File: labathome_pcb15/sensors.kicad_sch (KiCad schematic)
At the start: 23 parts, among them J12 TCS34725, J16 BMEx80, J19 BH1750, J20 CCS811, J21 QWIIC, J23 VL53L5x, J4 SCD4x, U12 AHT20, U14 BMP280, U19 DS18B20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

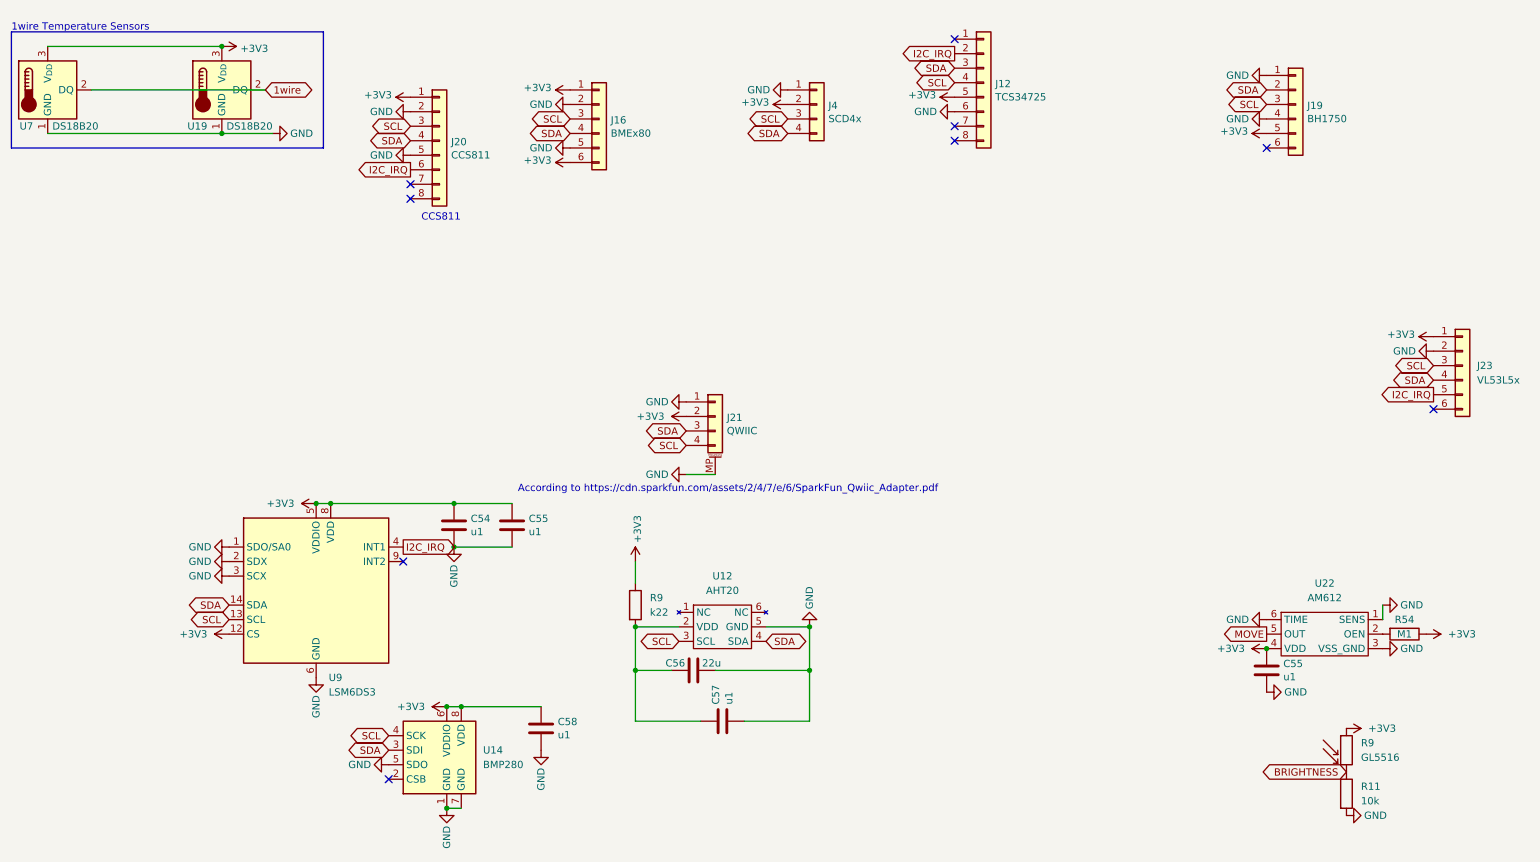
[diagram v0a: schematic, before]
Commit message: Updates in PCB, arduino test firmware
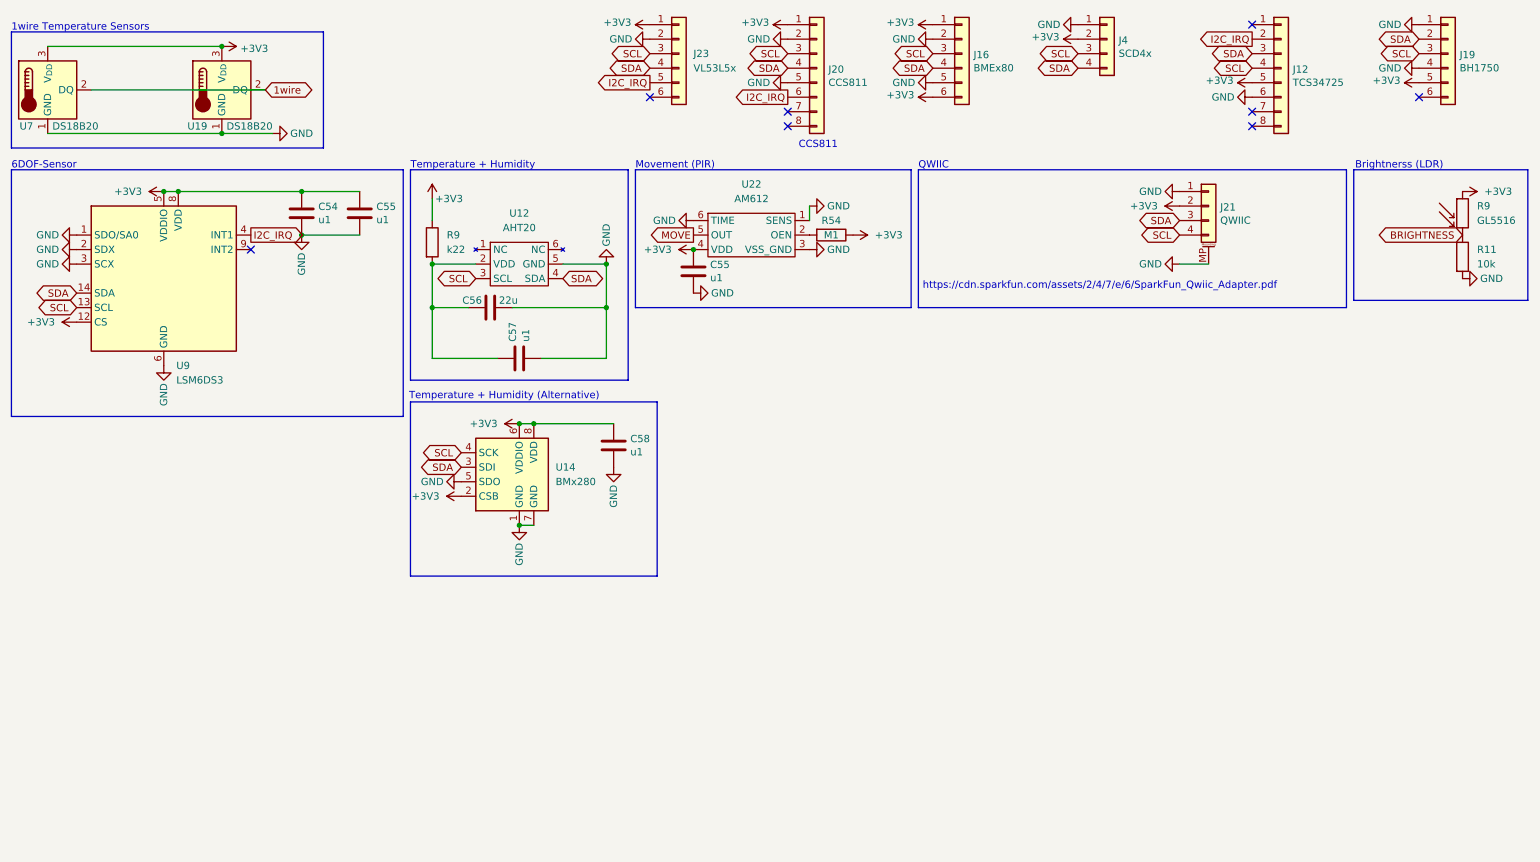
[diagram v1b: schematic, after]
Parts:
- U14: value BMP280 -> BMx280
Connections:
- net +3V3: now also U14.2 (CSB)
- no-connect marks 9 -> 8
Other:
- note added: "6DOF-Sensor"
- note added: "Brightnerss (LDR)"
- note added: "Movement (PIR)"
- note added: "QWIIC"
- note added: "Temperature + Humidity"
- note added: "Temperature + Humidity (Alternative)"
- note added: "https://cdn.sparkfun.com/assets/2/4/7/e/6/SparkFun_Qwiic_Adapter.pdf"
- note removed: "According to https://cdn.sparkfun.com/assets/2/4/7/e/6/SparkFun_Qwiic_Adapter.pdf"
- company: (none) -> Klaus Liebler
- title: (none) -> lab@home
- moved on the sheet: C54, C55, C56, C57, C58, J12, J16, J19, J20, J21, J23, J4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

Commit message: Various last minute
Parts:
- C54, C55, C57, C58: footprint Capacitor_SMD:C_0402_1005Metric -> Capacitor_SMD:C_0201_0603Metric
- R11: footprint Resistor_SMD:R_0402_1005Metric -> Resistor_SMD:R_0201_0603Metric
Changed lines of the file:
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@@
 			)
 		)
-		(property "Footprint" "Capacitor_SMD:C_0402_1005Metric"
+		(property "Footprint" "Capacitor_SMD:C_0201_0603Metric"
 			(at 137.4648 55.88 0)
 			(effects
@@
 			)
 		)
-		(property "Footprint" "Capacitor_SMD:C_0402_1005Metric"
+		(property "Footprint" "Capacitor_SMD:C_0201_0603Metric"
 			(at 104.14 75.8952 0)
 			(effects
@@
 			)
 		)
-		(property "Footprint" "Capacitor_SMD:C_0402_1005Metric"
+		(property "Footprint" "Capacitor_SMD:C_0201_0603Metric"
 			(at 123.4948 86.36 0)
 			(effects
@@
 			)
 		)
-		(property "Footprint" "Resistor_SMD:R_0402_1005Metric"
+		(property "Footprint" "Resistor_SMD:R_0201_0603Metric"
 			(at 271.272 57.15 90)
 			(effects
@@
 			)
 		)
-		(property "Footprint" "Capacitor_SMD:C_0402_1005Metric"
+		(property "Footprint" "Capacitor_SMD:C_0201_0603Metric"
 			(at 68.8848 45.72 0)
 			(effects

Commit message: 4 Layers
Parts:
- C55: footprint Capacitor_SMD:C_0402_1005Metric -> Capacitor_SMD:C_0201_0603Metric
- R54: footprint Resistor_SMD:R_0402_1005Metric -> Resistor_SMD:R_0201_0603Metric
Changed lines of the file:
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@@
 			)
 		)
-		(property "Footprint" "Capacitor_SMD:C_0402_1005Metric"
+		(property "Footprint" "Capacitor_SMD:C_0201_0603Metric"
 			(at 79.0448 45.72 0)
 			(effects
@@
 			)
 		)
-		(property "Footprint" "Resistor_SMD:R_0402_1005Metric"
+		(property "Footprint" "Resistor_SMD:R_0201_0603Metric"
 			(at 162.56 51.562 90)
 			(effects

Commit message: Pushed microSD up
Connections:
- net +3V3: no longer J16.6 (Pin_6)
- net GND: no longer J16.5 (Pin_5)
- no-connect marks 8 -> 10
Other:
- note added: "CS"
- note added: "SDO"
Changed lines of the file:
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@@
 	)
 	(no_connect
+		(at 180.34 29.21)
+	)
+	(no_connect
 		(at 154.94 31.75)
 	)
@@
 		(at 236.22 31.75)
 	)
+	(no_connect
+		(at 180.34 26.67)
+	)
 	(wire
 		(pts
@@
 		)
 	)
+	(text "CS"
+		(exclude_from_sim no)
+		(at 188.976 29.464 0)
+		(effects
+			(font
+				(size 1.27 1.27)
+			)
+		)
+	)
+	(text "SDO"
+		(exclude_from_sim no)
+		(at 188.976 26.924 0)
+		(effects
+			(font
+				(size 1.27 1.27)
+			)
+		)
+	)
 	(global_label "SCL"
 		(shape bidirectional)
@@
 	)
 	(symbol
-		(lib_id "power:GND")
-		(at 180.34 26.67 270)
-		(unit 1)
-		(exclude_from_sim no)
-		(in_bom yes)
-		(on_board yes)
-		(dnp no)
-		(property "Reference" "#PWR0138"
-			(at 173.99 26.67 0)
-			(effects
-				(font
-					(size 1.27 1.27)
-				)
-				(hide yes)
-			)
-		)
-		(property "Value" "GND"
-			(at 175.26 26.67 90)
-			(effects
-				(font
-					(size 1.27 1.27)
-				)
-			)
-		)
-		(property "Footprint" ""
-			(at 180.34 26.67 0)
-			(effects
-				(font
-					(size 1.27 1.27)
-				)
-				(hide yes)
-			)
-		)
-		(property "Datasheet" ""
-			(at 180.34 26.67 0)
-			(effects
-				(font
-					(size 1.27 1.27)
-				)
-				(hide yes)
-			)
-		)
-		(property "Description" "Power symbol creates a global label with name \"GND\" , ground"
-			(at 180.34 26.67 0)
-			(effects
-				(font
-					(size 1.27 1.27)
-				)
-				(hide yes)
-			)
-		)
-		(pin "1"
-		)
-		(instances
-			(project "labathome_pcb15"
-				(path "/e4d6926a-1a8b-424d-97c4-66b6ad87e4ac/faeff10d-104f-4ca8-a480-26bd51140cf0"
-					(reference "#PWR0138")
-					(unit 1)
-				)
-			)
-		)
-	)
-	(symbol
 		(lib_id "Connector_Generic_MountingPin:Conn_01x04_MountingPin")
 		(at 228.6 48.26 0)
@@
 					(unit 1)
 				)
-			)
-		)
-	)
-	(symbol
-		(lib_id "power:+3V3")
-		(at 180.34 29.21 90)
-		(unit 1)
-		(exclude_from_sim no)
-		(in_bom yes)
-		(on_board yes)
-		(dnp no)
-		(property "Reference" "#PWR0139"
-			(at 184.15 29.21 0)
-			(effects
-				(font
-					(size 1.27 1.27)
-				)
-				(hide yes)
-			)
-		)
-		(property "Value" "+3V3"
-			(at 177.0888 28.829 90)
-			(effects
-				(font
-					(size 1.27 1.27)
-				)
-				(justify left)
-			)
-		)
-		(property "Footprint" ""
-			(at 180.34 29.21 0)
-			(effects
-				(font
-					(size 1.27 1.27)
-				)
-				(hide yes)
-			)
-		)
-		(property "Datasheet" ""
-			(at 180.34 29.21 0)
-			(effects
-				(font
-					(size 1.27 1.27)
-				)
-				(hide yes)
-			)
-		)
-		(property "Description" "Power symbol creates a global label with name \"+3V3\""
-			(at 180.34 29.21 0)
-			(effects
-				(font
-					(size 1.27 1.27)
-				)
-				(hide yes)
-			)
-		)
-		(pin "1"
-		)
-		(instances
-			(project "labathome_pcb15"
-				(path "/e4d6926a-1a8b-424d-97c4-66b6ad87e4ac/faeff10d-104f-4ca8-a480-26bd51140cf0"
-					(reference "#PWR0139")
-					(unit 1)
-				)

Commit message: bsec
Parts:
- removed C58: u1, Capacitor_SMD:C_0201_0603Metric, symbol Device:C
- removed U14: BMx280, Package_LGA:Bosch_LGA-8_2x2.5mm_P0.65mm_ClockwisePinNumbering, symbol Sensor_Pressure:BMP280
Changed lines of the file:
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@@
-	)
-	(junction
-		(at 107.95 86.36)
-		(diameter 0)
-		(color 0 0 0 0)
 	)
 	(junction
@@
 	)
 	(junction
-		(at 110.49 86.36)
-		(diameter 0)
-		(color 0 0 0 0)
-	)
-	(junction
-		(at 107.95 104.14)
-		(diameter 0)
-		(color 0 0 0 0)
-	)
-	(junction
 		(at 123.19 58.42)
 		(diameter 0)
@@
 	(wire
 		(pts
-			(xy 110.49 86.36) (xy 124.46 86.36)
+			(xy 92.71 58.42) (xy 92.71 66.04)
 		)
 		(stroke
@@
 	(wire
 		(pts
-			(xy 92.71 58.42) (xy 92.71 66.04)
+			(xy 106.68 66.04) (xy 123.19 66.04)
 		)
 		(stroke
@@
 	(wire
 		(pts
-			(xy 106.68 66.04) (xy 123.19 66.04)
+			(xy 158.75 48.26) (xy 158.75 50.8)
 		)
 		(stroke
@@
 	(wire
 		(pts
-			(xy 158.75 48.26) (xy 158.75 50.8)
+			(xy 92.71 66.04) (xy 99.06 66.04)
 		)
 		(stroke
@@
 	(wire
 		(pts
-			(xy 92.71 66.04) (xy 99.06 66.04)
+			(xy 223.52 58.42) (xy 228.6 58.42)
 		)
 		(stroke
@@
 	(wire
 		(pts
-			(xy 223.52 58.42) (xy 228.6 58.42)
+			(xy 123.19 58.42) (xy 123.19 66.04)
 		)
 		(stroke
@@
 	(wire
 		(pts
-			(xy 123.19 58.42) (xy 123.19 66.04)
+			(xy 100.33 58.42) (xy 92.71 58.42)
 		)
 		(stroke
@@
 	(wire
 		(pts
-			(xy 100.33 58.42) (xy 92.71 58.42)
+			(xy 115.57 58.42) (xy 123.19 58.42)
 		)
 		(stroke
@@
 	(wire
 		(pts
-			(xy 115.57 58.42) (xy 123.19 58.42)
-		)
-		(stroke
-			(width 0)
-			(type default)
-		)
-	)
-	(wire
-		(pts
-			(xy 107.95 86.36) (xy 110.49 86.36)
+			(xy 107.95 86.36) (xy 124.46 86.36)
 		)
 		(stroke
@@
 	)
 	(symbol
-		(lib_id "Sensor_Pressure:BMP280")
-		(at 107.95 96.52 0)
-		(unit 1)
-		(exclude_from_sim no)
-		(in_bom yes)
-		(on_board yes)
-		(dnp no)
-		(fields_autoplaced yes)
-		(property "Reference" "U14"
-			(at 114.3 93.9799 0)
-			(effects
-				(font
-					(size 1.27 1.27)
-				)
-				(justify left)
-			)
-		)
-		(property "Value" "BMx280"
-			(at 114.3 96.5199 0)
-			(effects
-				(font
-					(size 1.27 1.27)
-				)
-				(justify left)
-			)
-		)
-		(property "Footprint" "Package_LGA:Bosch_LGA-8_2x2.5mm_P0.65mm_ClockwisePinNumbering"
-			(at 107.95 114.3 0)
-			(effects
-				(font
-					(size 1.27 1.27)
-				)
-				(hide yes)
-			)
-		)
-		(property "Datasheet" "https://ae-bst.resource.bosch.com/media/_tech/media/datasheets/BST-BMP280-DS001.pdf"
-			(at 107.95 96.52 0)
-			(effects
-				(font
-					(size 1.27 1.27)
-				)
-				(hide yes)
-			)
-		)
-		(property "Description" "Absolute Barometric Pressure Sensor, LGA-8"
-			(at 107.95 96.52 0)
-			(effects
-				(font
-					(size 1.27 1.27)
-				)
-				(hide yes)
-			)
-		)
-		(pin "8"
-		)
-		(pin "5"
-		)
-		(pin "2"
-		)
-		(pin "3"
-		)
-		(pin "1"
-		)
-		(pin "6"
-		)
-		(pin "4"
-		)
-		(pin "7"
-		)
-		(instances
-			(project "labathome_pcb15"
-				(path "/e4d6926a-1a8b-424d-97c4-66b6ad87e4ac/faeff10d-104f-4ca8-a480-26bd51140cf0"
-					(reference "U14")
-					(unit 1)
-				)
-			)
-		)
-	)
-	(symbol
 		(lib_id "power:GND")
 		(at 45.72 76.2 0)
@@
 					(unit 1)
 				)
-			)
-		)
-	)
-	(symbol
-		(lib_id "Device:C")
-		(at 124.46 90.17 180)
-		(unit 1)
-		(exclude_from_sim no)
-		(in_bom yes)
-		(on_board yes)
-		(dnp no)
-		(property "Reference" "C58"
-			(at 127.381 89.0016 0)
-			(effects
-				(font
-					(size 1.27 1.27)
-				)
-				(justify right)
-			)
-		)
-		(property "Value" "u1"
-			(at 127.381 91.313 0)
-			(effects
-				(font
-					(size 1.27 1.27)
-				)
-				(justify right)
-			)
-		)
-		(property "Footprint" "Capacitor_SMD:C_0201_0603Metric"
-			(at 123.4948 86.36 0)
-			(effects
-				(font
-					(size 1.27 1.27)
-				)
-				(hide yes)
-			)
-		)
-		(property "Datasheet" "~"
-			(at 124.46 90.17 0)
-			(effects
-				(font
-					(size 1.27 1.27)
-				)
-				(hide yes)
-			)
-		)
-		(property "Description" ""
-			(at 124.46 90.17 0)
-			(effects
-				(font
-					(size 1.27 1.27)
-				)
-				(hide yes)
-			)
-		)
-		(property "Option" "MS4525DO"
-			(at 124.46 90.17 0)
-			(effects
-				(font
-					(size 1.27 1.27)
-				)
-				(hide yes)
-			)
-		)
-		(pin "1"
-		)
-		(pin "2"
-		)
-		(instances
-			(project "labathome_pcb15"
-				(path "/e4d6926a-1a8b-424d-97c4-66b6ad87e4ac/faeff10d-104f-4ca8-a480-26bd51140cf0"
-					(reference "C58")
-					(unit 1)
-				)
